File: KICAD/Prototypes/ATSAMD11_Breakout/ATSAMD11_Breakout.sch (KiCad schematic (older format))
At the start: 11 parts

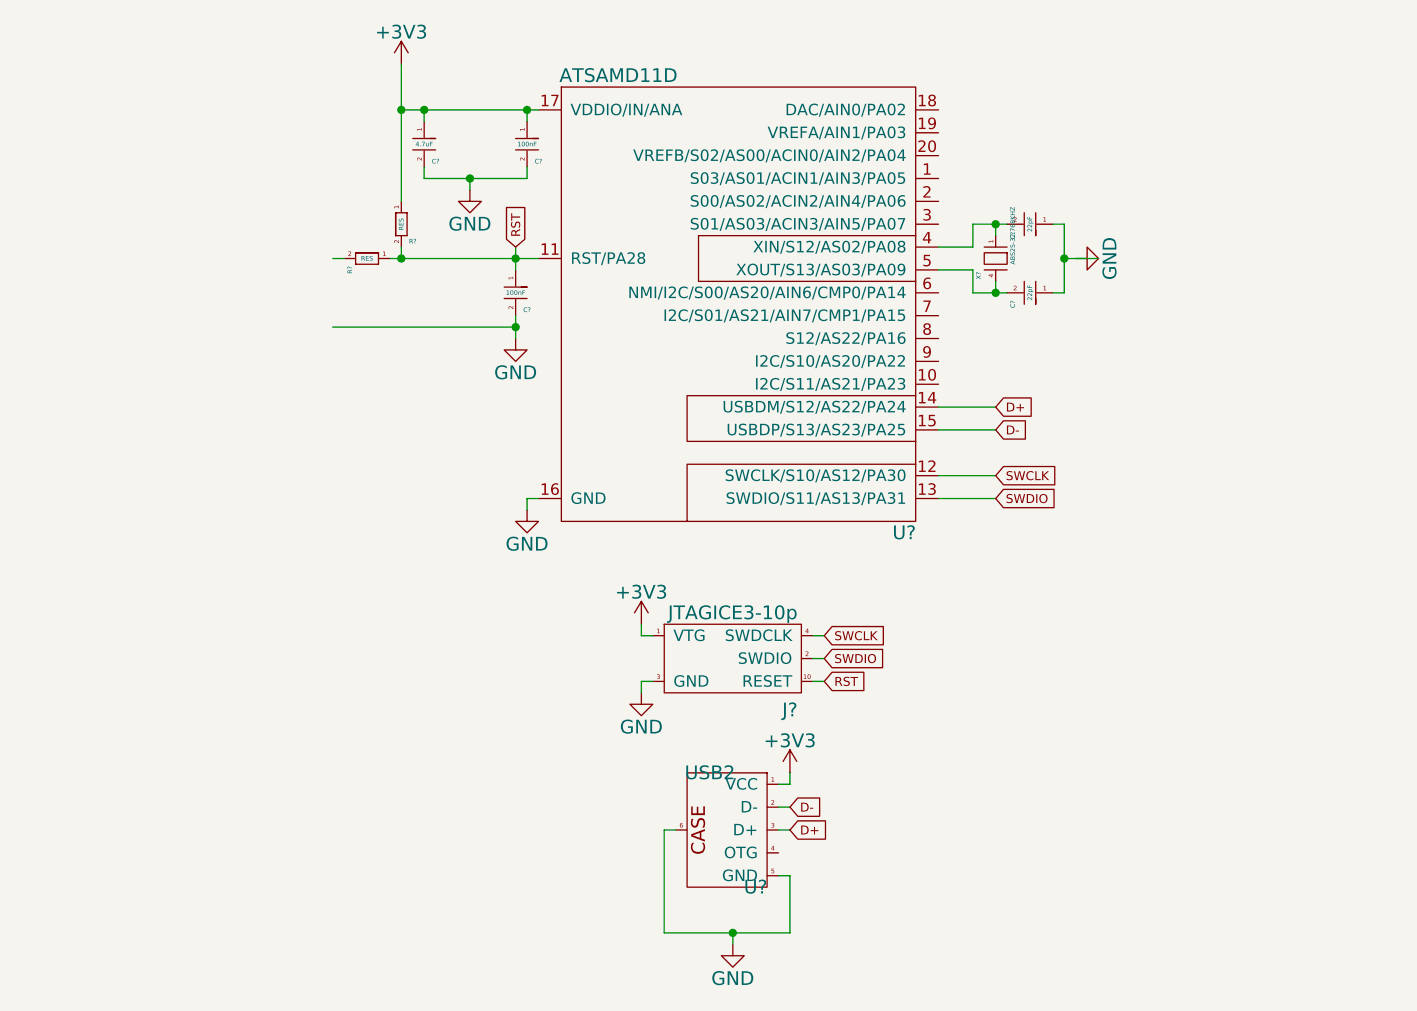
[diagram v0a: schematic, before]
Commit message: Added ATSAMD11 breakout
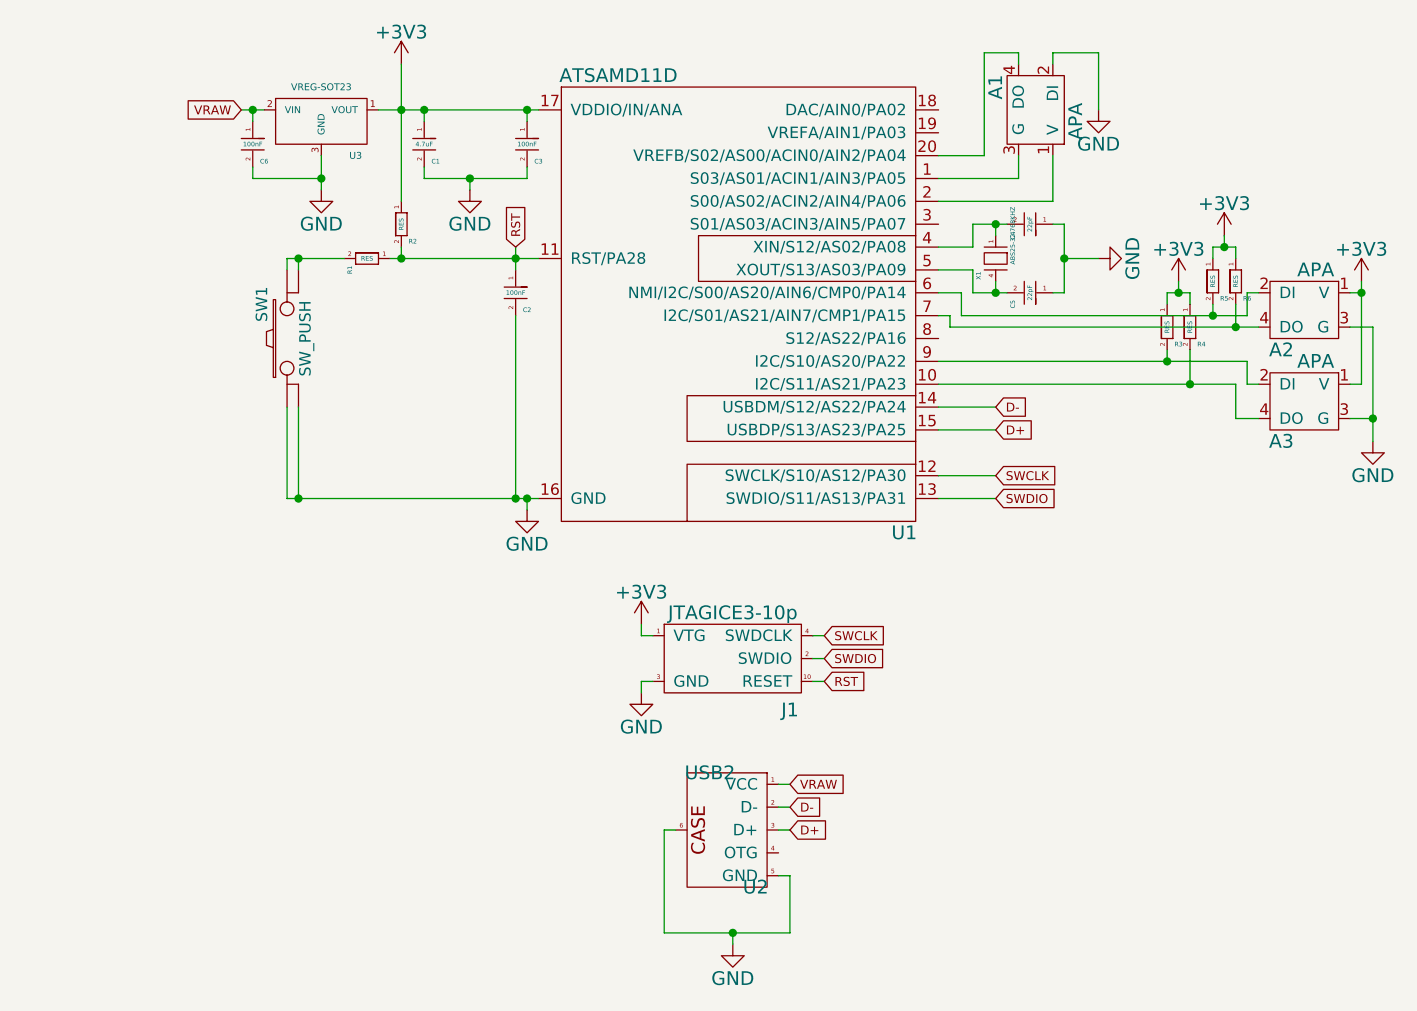
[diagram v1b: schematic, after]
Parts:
- added A1, A2, A3: APA, _Fab_Footprint:SMD-Header-2x2, symbol APA
- added C6: 100nF, _Fab_Footprint:CAP_1206_FAB, symbol CAP
- added R3, R4, R5, R6: RES, _Fab_Footprint:CAP_1206_FAB, symbol RES
- added SW1: SW_PUSH, _Fab_Footprint:Switch-Tactile-B3SN-3112P, symbol SW_PUSH
- added U3: VREG-SOT23, TO_SOT_Packages_SMD:SOT-23, symbol VREG-SOT23
- C1, C2, C3, C4, C5: renamed from C?; footprint (none) -> _Fab_Footprint:CAP_1206_FAB
- J1: renamed from J?; footprint (none) -> _Fab_Footprint:JTAGICE3-10p
- R1, R2: renamed from R?; footprint (none) -> _Fab_Footprint:CAP_1206_FAB
- U1: renamed from U?; footprint (none) -> Housings_SOIC:SOIC-20W_7.5x12.8mm_Pitch1.27mm
- U2: renamed from U?; footprint (none) -> _Fab_Footprint:USBMINIB2.0
- X1: renamed from X?; footprint (none) -> _Fab_Footprint:4-SOJ
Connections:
- net labels added: VRAW
- wire segments 61 -> 99

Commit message: added RTC library, board defs derived from Mattairtech
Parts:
- added A4: APA, _Fab_Footprint:SMD-Header-2x2, symbol APA
- added L1: FAB_LED, _Fab_Footprint:LED_1206_FAB, symbol FAB_LED
- added Q1: N-MOSFET, TO_SOT_Packages_SMD:SOT-23, symbol N-MOSFET
- added R7: RES, _Fab_Footprint:CAP_1206_FAB, symbol RES
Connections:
- net GND: now also A4.2 (DI), A4.4 (DO), Q1.3
- net VRAW: now also A4.1 (V), A4.3 (G)
- net EN: now reaches U1.8 (S12/AS22/PA16)
- new net: L1.1, R7.2
- new net: L1.2, Q1.2
